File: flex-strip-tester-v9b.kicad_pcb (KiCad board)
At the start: 2 copper layers, 65.9 x 25 mm, 10 parts, among them J2 Conn_01x01_Female

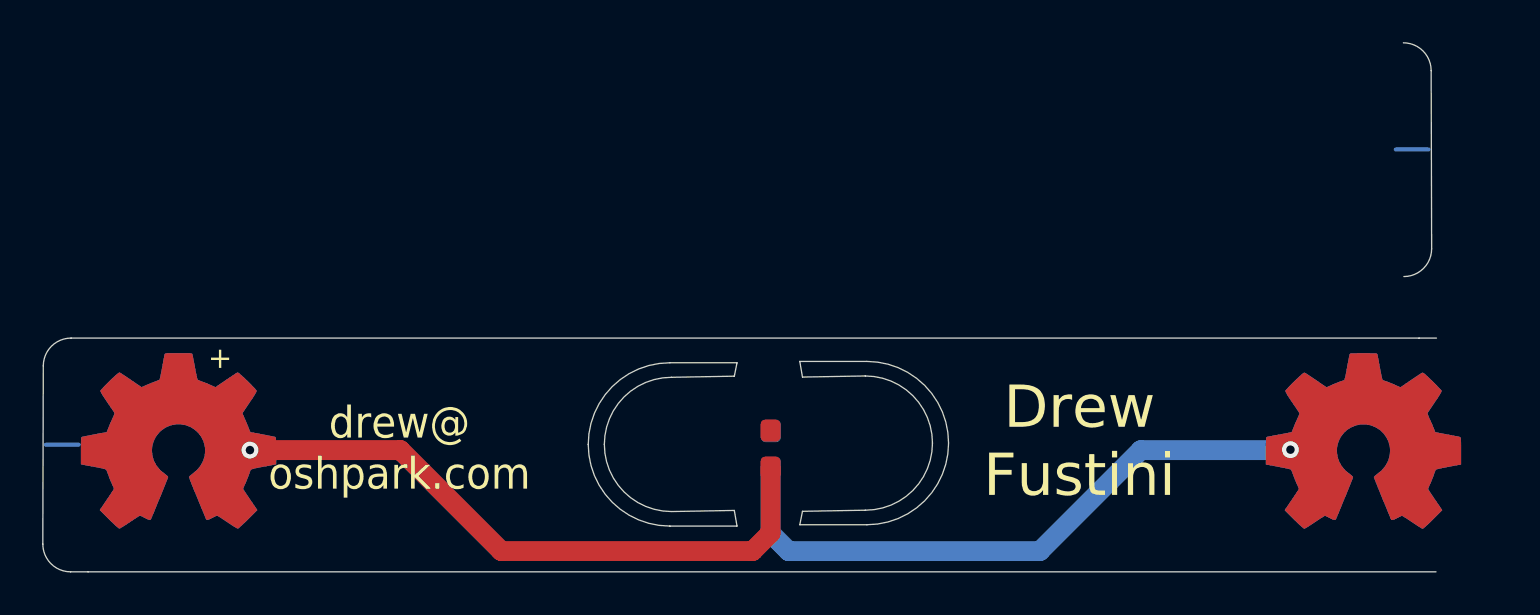
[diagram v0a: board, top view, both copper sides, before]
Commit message: rework cutout and add oshw logo to center
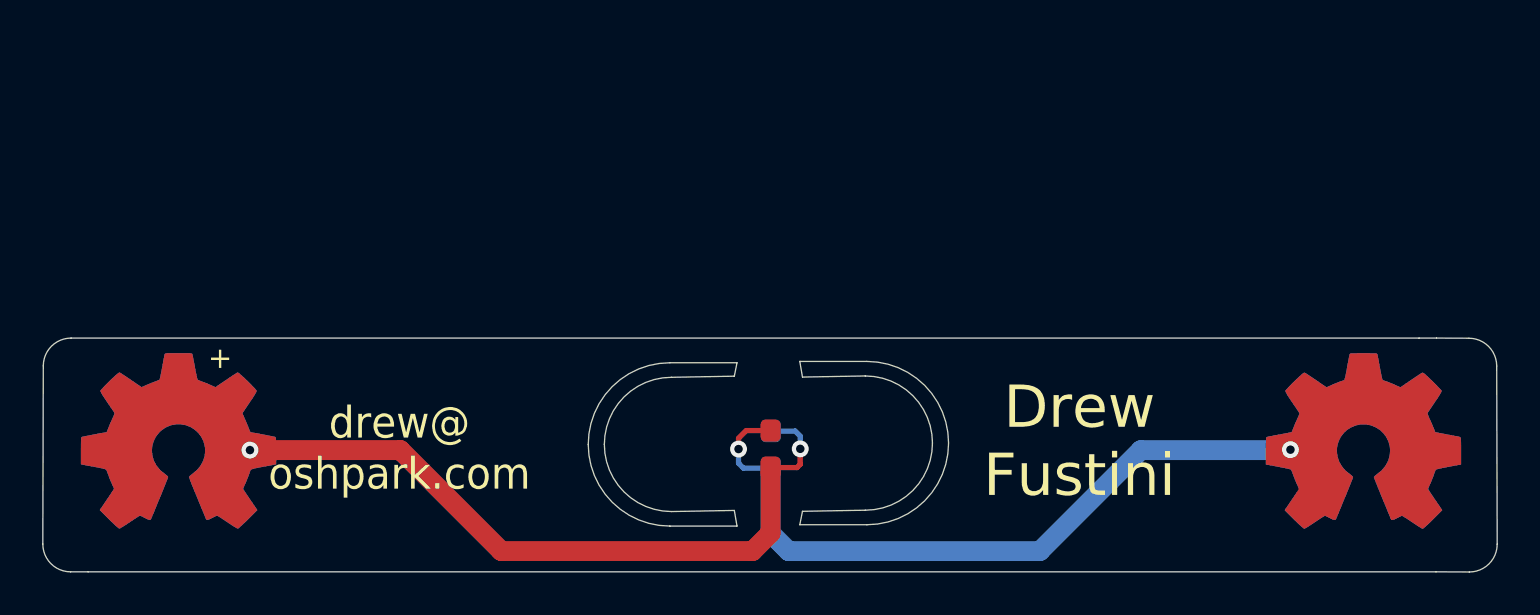
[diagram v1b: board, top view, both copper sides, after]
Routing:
- net +3V3: track 30.1 -> 34.6 mm, vias 1 -> 2
- net GND: track 30.1 -> 34.3 mm, vias 1 -> 2
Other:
- board size 65.9 x 25 mm -> 68.8 x 11.1 mm
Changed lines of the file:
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@@
   (general
     (thickness 0.1)
-    (drawings 54)
-    (tracks 12)
+    (drawings 53)
+    (tracks 27)
     (modules 10)
     (nets 3)
@@
       (drillshape 0)
       (scaleselection 1)
-      (outputdirectory "")
+      (outputdirectory "gerber/")
     )
   )
@@
     )
   )
+  (gr_line (start 118.89 95.43) (end 153.23 95.43) (layer "B.Fab") (width 0.1))
+  (gr_line (start 151.7015 92.075) (end 151.7015 98.425) (layer "Eco2.User") (width 0.1))
+  (gr_line (start 184.72404 90.23096) (end 186.25714 90.238094) (layer "Edge.Cuts") (width 0.05))
+  (gr_line (start 184.70118 101.28758) (end 186.28 101.294714) (layer "Edge.Cuts") (width 0.05))
   (gr_line (start 246.30908 101.29) (end 182.55 101.29) (layer "Eco1.User") (width 0.05))
-  (gr_arc (start 183.156716 77.579212) (end 183.156716 76.264498) (angle 90) (layer "Edge.Cuts") (width 0.05))
-  (gr_arc (start 183.179576 86.006404) (end 183.179576 87.321118) (angle -90) (layer "Edge.Cuts") (width 0.05))
-  (gr_line (start 184.47143 77.579212) (end 184.49429 86.006404) (layer "Edge.Cuts") (width 0.05))
-  (gr_line (start 184.347976 81.308938) (end 182.798576 81.308938) (layer "B.Cu") (width 0.2))
+  (gr_arc (start 186.25714 91.552808) (end 186.25714 90.238094) (angle 90) (layer "Edge.Cuts") (width 0.05))
+  (gr_arc (start 186.28 99.98) (end 186.28 101.294714) (angle -90) (layer "Edge.Cuts") (width 0.05))
+  (gr_line (start 187.571854 91.552808) (end 187.594714 99.98) (layer "Edge.Cuts") (width 0.05))
   (gr_line (start 153.23 95.43) (end 187.57 95.43) (layer "F.Fab") (width 0.1))
-  (gr_line (start 118.89 95.43) (end 153.23 95.43) (layer "B.Fab") (width 0.1))
   (gr_line (start 146.06 100.83) (end 186.9286 100.83) (layer "B.Fab") (width 0.1))
-  (dimension 5.22224 (width 0.12) (layer "F.SilkS")
-    (gr_text "5.222 mm" (at 197.77964 92.85224 90) (layer "F.SilkS")
-      (effects (font (size 1 1) (thickness 0.15)))
-    )
-    (feature1 (pts (xy 117.17274 90.24112) (xy 197.096061 90.24112)))
-    (feature2 (pts (xy 117.17274 95.46336) (xy 197.096061 95.46336)))
-    (crossbar (pts (xy 196.50964 95.46336) (xy 196.50964 90.24112)))
-    (arrow1a (pts (xy 196.50964 90.24112) (xy 197.096061 91.367624)))
-    (arrow1b (pts (xy 196.50964 90.24112) (xy 195.923219 91.367624)))
-    (arrow2a (pts (xy 196.50964 95.46336) (xy 197.096061 94.336856)))
-    (arrow2b (pts (xy 196.50964 95.46336) (xy 195.923219 94.336856)))
-  )
   (gr_text "Drew\nFustini" (at 167.83558 95.11284) (layer "F.SilkS")
     (effects (font (size 2 2) (thickness 0.3)))
@@
   (gr_line (start 151.7015 98.425) (end 151.7015 99.06) (layer "Eco1.User") (width 0.1))
   (gr_line (start 152.347446 99.1235) (end 151.648946 99.1235) (layer "Eco1.User") (width 0.1))
-  (gr_line (start 118.9482 95.2754) (end 120.4976 95.2754) (layer "B.Cu") (width 0.2))
   (gr_line (start 155.2575 99.06) (end 154.6225 99.06) (layer "Eco1.User") (width 0.1))
   (gr_line (start 156.220946 98.4885) (end 133.233946 98.4885) (layer "Eco2.User") (width 0.1))
@@
   (gr_line (start 154.734169 98.425) (end 154.607169 99.06) (layer "Edge.Cuts") (width 0.05))
   (gr_line (start 157.707723 98.372446) (end 154.734169 98.425) (layer "Edge.Cuts") (width 0.05))
-  (gr_line (start 151.7015 92.075) (end 151.7015 98.425) (layer "Eco2.User") (width 0.1))
   (gr_line (start 154.6225 92.0115) (end 154.6225 98.3615) (layer "Eco2.User") (width 0.1))
   (gr_line (start 156.220946 99.1235) (end 133.233946 99.1235) (layer "Eco2.User") (width 0.1))
@@
     (effects (font (size 1 1) (thickness 0.15)) (justify mirror))
   )
+  (segment (start 154.63 95.47) (end 154.63 94.87) (width 0.25) (layer "B.Cu") (net 1))
+  (segment (start 154.63 94.87) (end 154.389 94.629) (width 0.25) (layer "B.Cu") (net 1))
+  (segment (start 154.389 94.629) (end 153.2382 94.629) (width 0.25) (layer "B.Cu") (net 1))
+  (segment (start 153.2255 96.35614) (end 154.47386 96.35614) (width 0.25) (layer "F.Cu") (net 1))
+  (segment (start 154.47386 96.35614) (end 154.63 96.2) (width 0.25) (layer "F.Cu") (net 1))
+  (segment (start 154.63 96.2) (end 154.63 95.47) (width 0.25) (layer "F.Cu") (net 1))
+  (segment (start 151.71 95.48) (end 151.71 94.97) (width 0.25) (layer "F.Cu") (net 2))
+  (segment (start 151.71 94.97) (end 152.07386 94.60614) (width 0.25) (layer "F.Cu") (net 2))
+  (segment (start 152.07386 94.60614) (end 153.2255 94.60614) (width 0.25) (layer "F.Cu") (net 2))
+  (segment (start 153.2382 96.379) (end 151.939 96.379) (width 0.25) (layer "B.Cu") (net 2))
+  (segment (start 151.71 96.15) (end 151.71 95.48) (width 0.25) (layer "B.Cu") (net 2))
+  (segment (start 151.939 96.379) (end 151.71 96.15) (width 0.25) (layer "B.Cu") (net 2))
+  (via (at 151.71 95.48) (size 0.8) (drill 0.4) (layers "F.Cu" "B.Cu") (net 2))
+  (via (at 154.63 95.47) (size 0.8) (drill 0.4) (layers "F.Cu" "B.Cu") (net 1))
+  (segment (start 153.27936 94.66) (end 153.2255 94.60614) (width 0.25) (layer "F.Cu") (net 2))
   (segment (start 165.96355 100.30635) (end 170.73875 95.53115) (width 0.9398) (layer "B.Cu") (net 2))
   (segment (start 170.75 95.53) (end 177.862 95.53) (width 0.9398) (layer "B.Cu") (net 2))
